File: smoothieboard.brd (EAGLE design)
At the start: 105.1 x 105.1 mm, 236 parts, among them IC10 LM1117-3.3V, IC2 A4982, IC3 A4982, IC4 MCP44X1, IC5 A4982, IC6 A4982, IC9 78L12Z, J10 POWER_JACKSMD, J5 POWER_JACKSMD, Q1 NP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

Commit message: give main IC value of LPC1769 to ease BOM generation
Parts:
- IC1: value (none) -> LPC1769
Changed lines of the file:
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@@
 </autorouter>
 <elements>
-<element name="IC1" library="microbuilder" package="LQFP100" value="" x="59.817" y="52.705" smashed="yes" rot="R45">
+<element name="IC1" library="microbuilder" package="LQFP100" value="LPC1769" x="59.817" y="52.705" smashed="yes" rot="R45">
 <attribute name="NAME" x="70.31055" y="52.361203125" size="1.016" layer="25" ratio="10"/>
 <attribute name="VALUE" x="73.287375" y="55.399071875" size="1.778" layer="27" ratio="10" rot="R135"/>

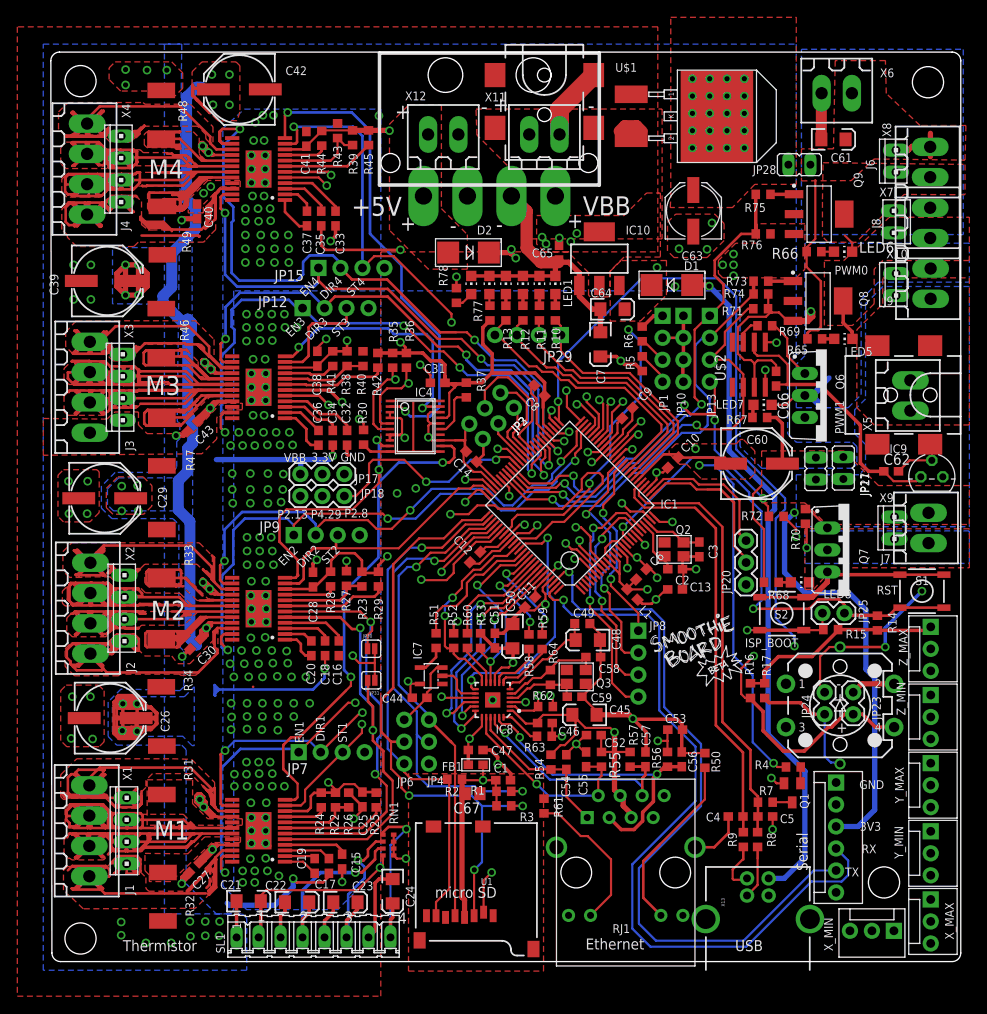
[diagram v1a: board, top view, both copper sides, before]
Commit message: switch 78L12Z for 78L12F surface mount package. also route remaining ratsnest wires- all were traces contacting pad, just not connected to center of pad
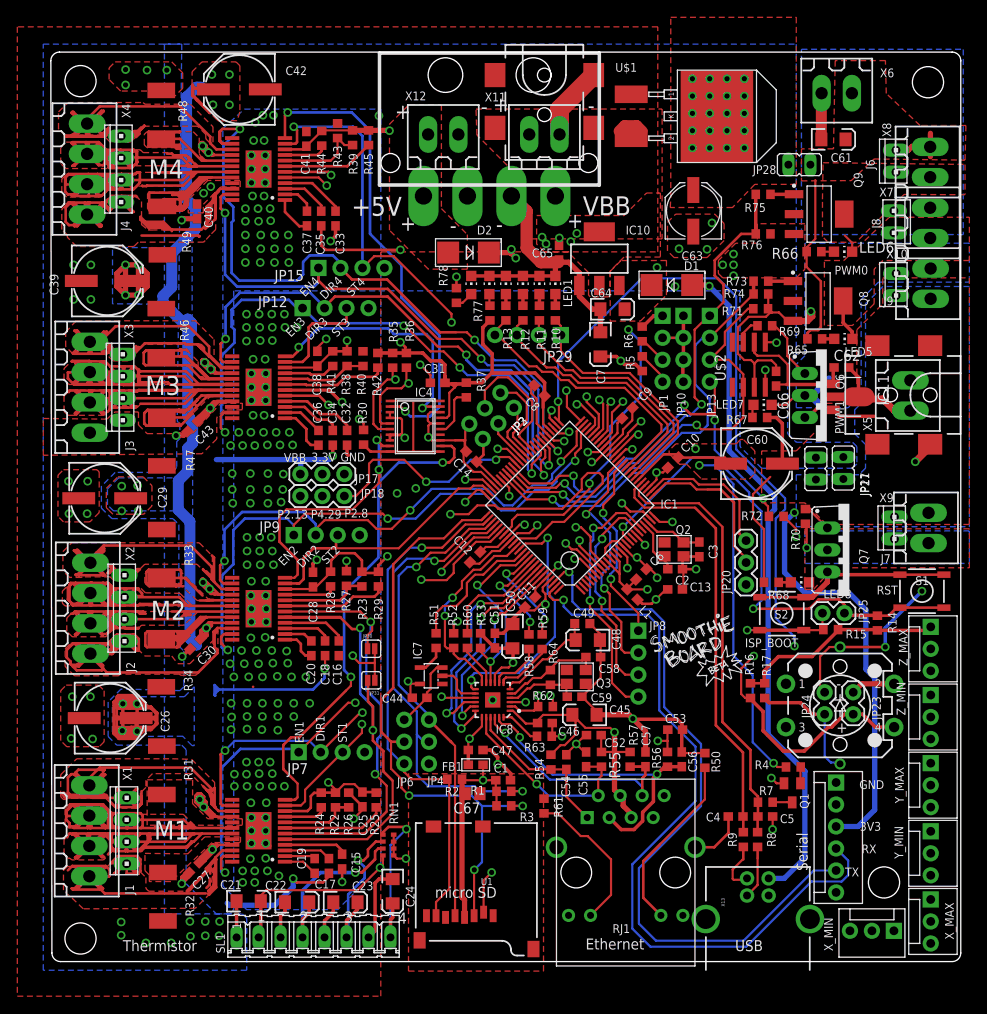
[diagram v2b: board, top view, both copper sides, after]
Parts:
- removed IC9: 78L12Z, linear:TO92
- added IC11: 78L12F, linear:SOT89
- moved C62 13.3 mm to (91.2, 68.6)
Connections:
- net 12VREG: now also IC11.1; no longer IC9.1
- net GND: now also IC11.2, IC11.2@1; no longer IC9.2
- net MOSFET_DRIVE: now also IC11.3; no longer IC9.3
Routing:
- net 12VREG: track 32.2 -> 16.6 mm
- net GND: track 309.3 -> 323.8 mm, vias 217 -> 218
- net MOSFET_DRIVE: track 18.8 -> 25.3 mm

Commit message: USB-B connector, solder jumper for 5v/3v3 UART power (NOT signals, they're always 3v3)
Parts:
- removed X13: USBPTH, SparkFun:USB-B-PTH
- added SJ1: (no value), SparkFun:SJ_3
- added X14: USBPTH, SparkFun:USB-B-PTH
- moved R9 5.26 mm to (82.1, 18.8)
- moved C4 5.14 mm to (83.7, 18.7), turned to 90 degrees
- moved R7 5.02 mm to (77.4, 18.8), turned to 270 degrees
- moved R8 4.85 mm to (80.5, 18.8)
- moved C5 3.98 mm to (79.0, 18.8), turned to 90 degrees
- moved JP5 2.02 mm to (92.6, 20.4)
- moved Q1 1.12 mm to (86.0, 20.5)
- moved R4 1.06 mm to (86.4, 23.2)
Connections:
- new net N$23: JP5.3, SJ1.2
- net 3.3V: now also SJ1.1
- net 5V: now also SJ1.3; no longer JP5.3
- net GND: now also X14.GND; no longer X13.GND
- net N$61: now also X14.D+; no longer X13.D+
- net N$62: now also X14.D-; no longer X13.D-
- net VUSB: now also X14.VBUS; no longer X13.VBUS
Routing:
- net 5V: track 91.1 -> 5.36 mm
- net N$23: track 0.00 -> 80.0 mm, vias 0 -> 2
- net RX_0: track 88.6 -> 63.8 mm, vias 1 -> 2
- net TX_0: track 84.2 -> 63.1 mm
- net GND: track 323.8 -> 307.9 mm, vias 218 -> 234
- net N$51: track 2.31 -> 12.5 mm, vias 0 -> 2
- net VUSB: track 78.4 -> 73.6 mm
- net MOSFET_DRIVE: track 25.3 -> 21.3 mm
- net USB_D+: track 49.6 -> 47.7 mm
- net X_MIN: track 77.7 -> 79.4 mm
- net N$62: track 6.01 -> 4.38 mm
- net USB_D-: track 49.4 -> 47.8 mm, vias 0 -> 2
- net N$61: track 6.21 -> 7.16 mm
- net N$73: track 14.7 -> 15.4 mm
- net P2.9: track 100.8 -> 101.4 mm
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
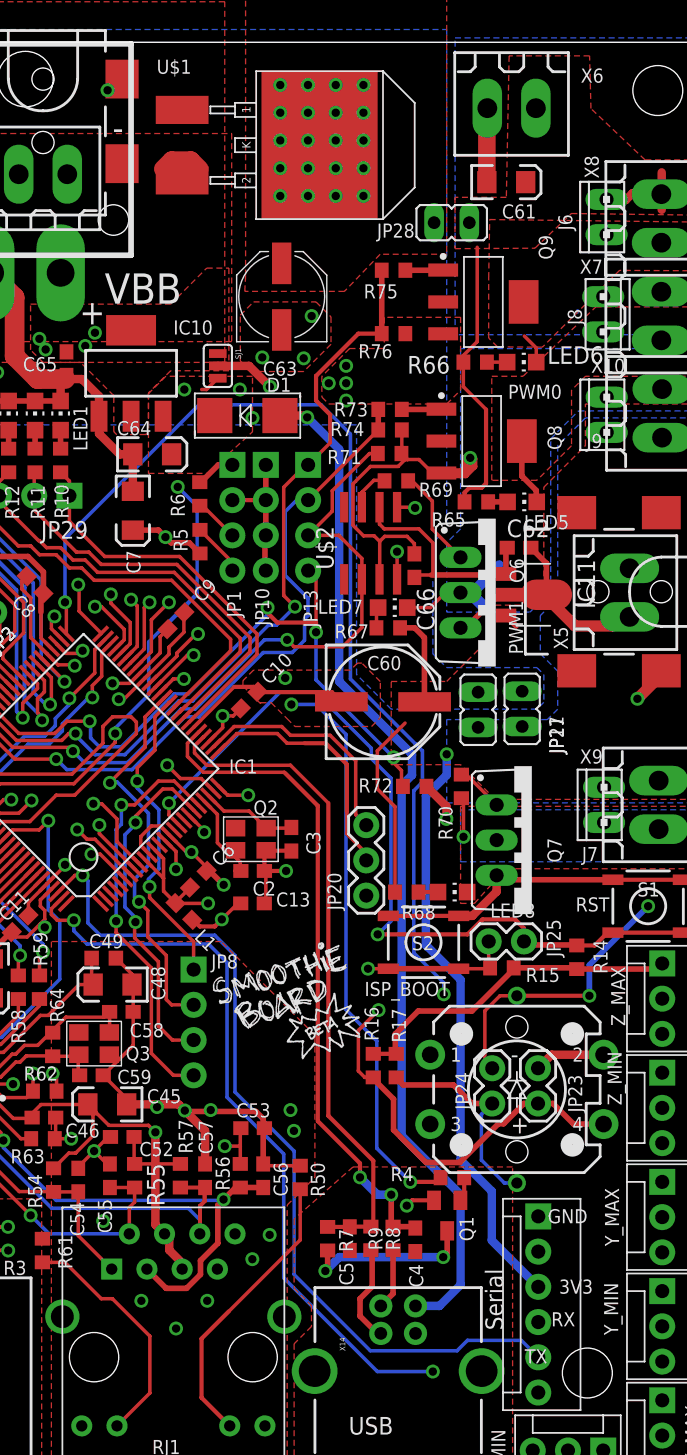
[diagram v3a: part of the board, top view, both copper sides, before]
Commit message: switch USB CONNECT transistor for a FET, move UART voltage selector next to UART header
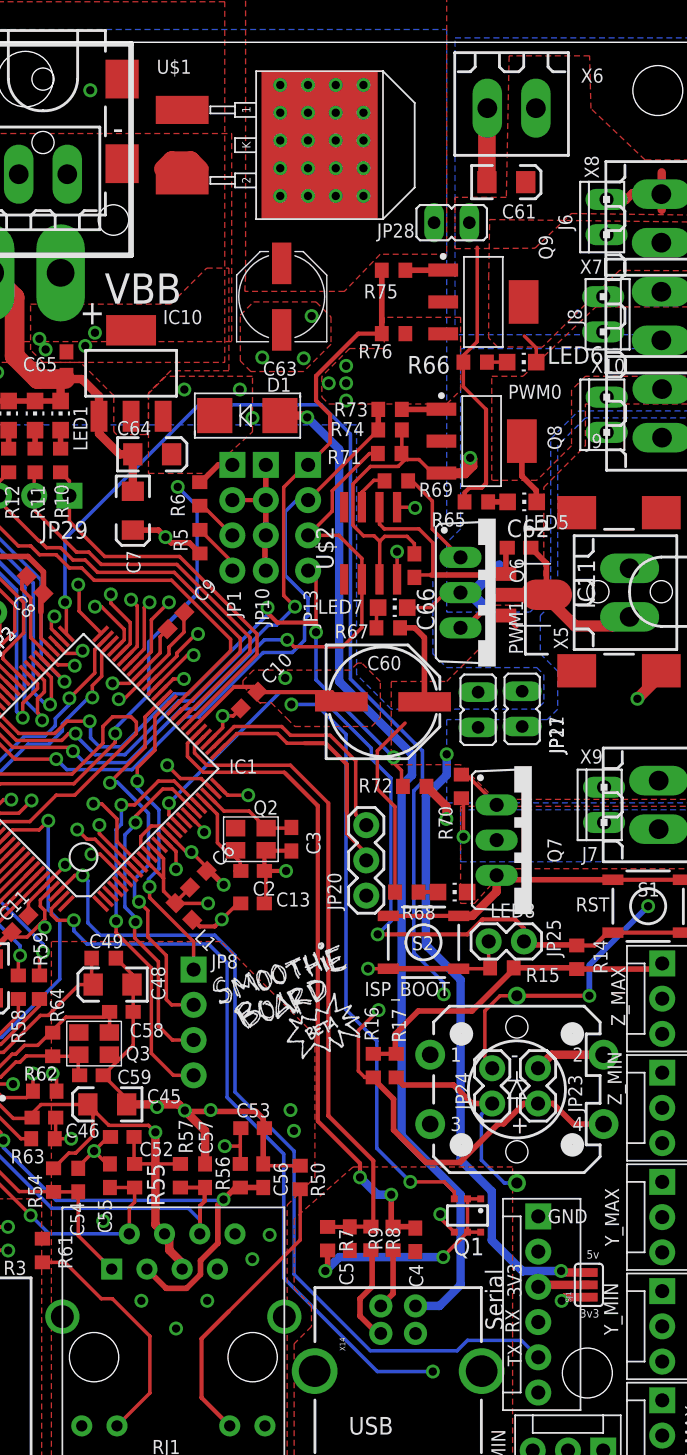
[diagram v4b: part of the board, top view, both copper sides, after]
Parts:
- removed R4: NP, resistor:R0603
- Q1: value NP -> BSL207SP; device transistor-pnp:SOT23-BEC -> transistor-fet:SC74_INFINEON
- moved SJ1 71.4 mm to (96.2, 15.5), turned to 90 degrees
- moved Q1 1.47 mm to (87.5, 20.5)
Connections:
- removed net N$59: Q1.B, R4.1
- net 3.3V: now also Q1.4; no longer Q1.E
- net N$51: now also Q1.1, Q1.2, Q1.5, Q1.6; no longer Q1.C
- net P2.9: now also Q1.3; no longer R4.2
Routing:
- net 5V: track 5.36 -> 85.0 mm, vias 4 -> 6
- net N$23: track 80.0 -> 3.71 mm, vias 2 -> 0
- net N$51: track 12.5 -> 17.3 mm
- net N$59: track 1.75 -> 0.00 mm
- net P2.9: track 101.4 -> 103.0 mm
- net 3.3V: track 248.0 -> 249.6 mm, vias 23 -> 24
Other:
- board text added: "3v3"
- board text added: "5v"
